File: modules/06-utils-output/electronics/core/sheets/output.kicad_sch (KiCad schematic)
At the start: 28 parts, among them U4 NE5532, U5 TL072

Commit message: Utils JLCPCB verified for v1.0
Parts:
- D_LIM_N1, D_LIM_P1, RV_LINE_OUT_LVL1, TP1, TP2, TP3: CHECKED YES -> (none)
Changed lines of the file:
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@@
 			)
 		)
-		(property "CHECKED" "YES"
+		(property "CHECKED" ""
 			(at 262.89 116.84 0)
 			(effects
@@
 			)
 		)
-		(property "CHECKED" "YES"
+		(property "CHECKED" ""
 			(at 137.16 77.47 90)
 			(effects
@@
 			)
 		)
-		(property "CHECKED" "YES"
+		(property "CHECKED" ""
 			(at 45.72 54.61 0)
 			(effects
@@
 			)
 		)
-		(property "CHECKED" "YES"
+		(property "CHECKED" ""
 			(at 39.37 60.96 0)
 			(effects
@@
 			)
 		)
-		(property "CHECKED" "YES"
+		(property "CHECKED" ""
 			(at 147.32 77.47 90)
 			(effects
@@
 			)
 		)
-		(property "CHECKED" "YES"
+		(property "CHECKED" ""
 			(at 265.43 57.15 0)
 			(effects

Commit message: Added Utils BOM
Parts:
- D_LIM_N1, D_LIM_P1: Vendor (none) -> Mouser
- RV_LINE_OUT_LVL1: Mouser Part no. (none) -> 774-06TR4AA103CP; Part URL https://mou.sr/4gcYhlU -> https://mou.sr/44pTlq5
- TP1, TP2, TP3: Vendor (none) -> -
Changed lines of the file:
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@@
 			)
 		)
+		(property "Vendor" "-"
+			(at 262.89 116.84 0)
+			(effects
+				(font
+					(size 1.27 1.27)
+				)
+				(hide yes)
+			)
+		)
 		(pin "1"
 		)
@@
 			)
 		)
-		(property "Vendor" ""
+		(property "Vendor" "Mouser"
 			(at 137.16 77.47 0)
 			(effects
@@
 			)
 		)
-		(property "Vendor" ""
+		(property "Vendor" "-"
 			(at 45.72 54.61 0)
 			(effects
@@
 			)
 		)
-		(property "Part URL" "https://mou.sr/4gcYhlU"
+		(property "Part URL" "https://mou.sr/44pTlq5"
 			(at 39.37 60.96 0)
 			(effects
@@
 			)
 		)
+		(property "Mouser Part no." "774-06TR4AA103CP"
+			(at 39.37 60.96 0)
+			(effects
+				(font
+					(size 1.27 1.27)
+				)
+				(hide yes)
+			)
+		)
 		(pin "1"
 		)
@@
 			)
 		)
-		(property "Vendor" ""
+		(property "Vendor" "Mouser"
 			(at 147.32 77.47 0)
 			(effects
@@
 			(at 265.43 57.15 0)
 			(effects
+				(font
+					(size 1.27 1.27)
+				)
+				(hide yes)
+			)
+		)
+		(property "Vendor" "-"
+			(at 265.43 57.15 0)
+			(effects

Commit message: Updated drive LED footprint on Utils Core
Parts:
- D_LIM_P1: footprint LED_THT:LED_D5.0mm -> Connector_PinHeader_2.54mm:PinHeader_1x02_P2.54mm_Vertical
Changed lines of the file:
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@@
 			)
 		)
-		(property "Footprint" "LED_THT:LED_D5.0mm"
+		(property "Footprint" "Connector_PinHeader_2.54mm:PinHeader_1x02_P2.54mm_Vertical"
 			(at 137.16 77.47 0)
 			(effects

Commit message: KiCAD version update - Utils
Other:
- company: (none) -> Shmøergh
- title: (none) -> Utils / Output Core
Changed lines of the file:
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@@
 	(generator_version "9.0")
 	(paper "A4")
+	(title_block
+		(title "Utils / Output Core")
+		(date "2026-02-21")
+		(rev "v1.1")
+		(company "Shmøergh")
+	)
 	(rectangle
 		(start 160.02 33.02)

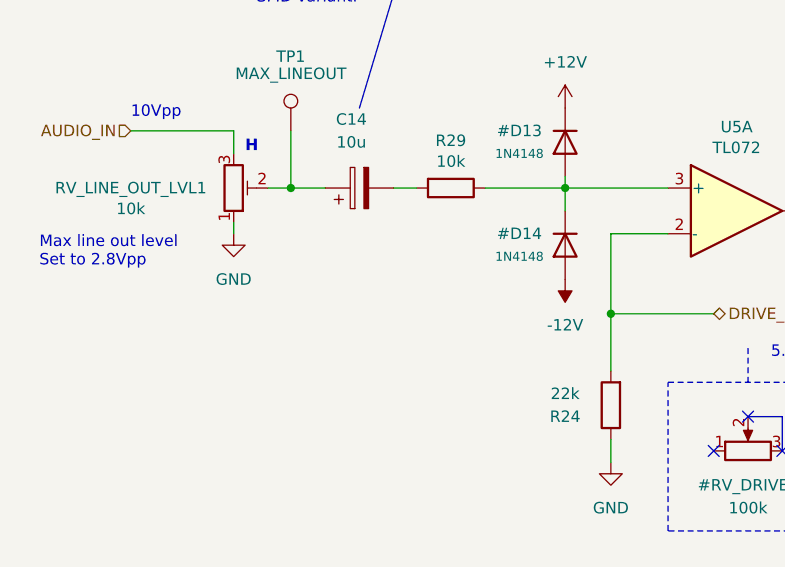
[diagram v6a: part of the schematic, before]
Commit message: Added 100k to GND on output opamp input
- In the first opamp stage of the Output (U5A), the opamp side was essentially floating. When there was a DC on the + node of C14 then that DC appeared on the - side too but had nowhere to discharge so essentially DC wasn't blocked properly. Inserting a 100k resistor to ground turns the input into a high pass filter with a cutoff frequence about 0.15Hz which discharges the DC component of the input. This is essential in the output stage of the synth.
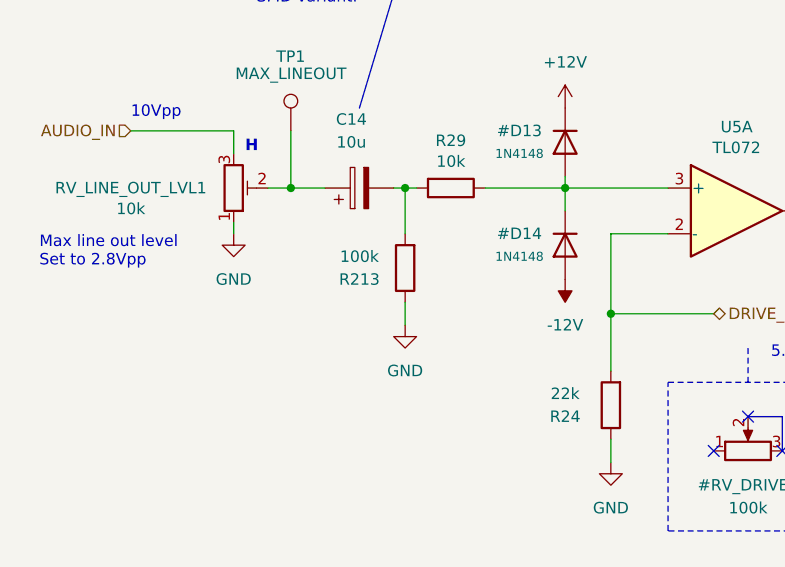
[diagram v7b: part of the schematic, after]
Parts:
- added R213: 100k, Resistor_SMD:R_0603_1608Metric, symbol Device:R
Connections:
- net GND: now also R213.1
- net at C14.2, R29.2: now also R213.2

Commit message: Removed comment in Outputs schemo
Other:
- note removed: "Proto this! If works, replace with SMD variant."
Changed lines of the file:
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@@
-		)
-	)
-	(text "Proto this! If works, replace with\nSMD variant."
-		(exclude_from_sim no)
-		(at 41.91 40.64 0)
-		(effects
-			(font
-				(size 1.27 1.27)
-				(color 255 0 255 1)
-			)
-			(justify left bottom)
 		)
 	)
@@
 		)
 	)
-	(polyline
-		(pts
-			(xy 53.34 52.07) (xy 57.15 39.37)
-		)
-		(stroke
-			(width 0)
-			(type solid)
-			(color 255 0 255 1)
-		)
-	)
